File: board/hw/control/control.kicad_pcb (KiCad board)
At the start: 2 copper layers, 54.3 x 82.5 mm, 41 parts, among them J1 stepper #1, J2 stepper #2, J3 buttons, J4 power, J6 AVR-ISP-10, Q1 MMFTP84W, Q2 MMFTP84W, U1 ULN2003A, U2 ULN2003A, U3 ULN2003A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

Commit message: vias for screws moved to MountingHole, so that it's clearly visible in 3D preview
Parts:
- added ?: M3, MountingHole:MountingHole_3.2mm_M3_Pad_TopBottom, F.Cu at (125.2, 67.5)
- added ?: M3, MountingHole:MountingHole_3.2mm_M3_Pad_TopBottom, F.Cu at (171.5, 67.5)
- added ?: M3, MountingHole:MountingHole_3.2mm_M3_Pad_TopBottom, F.Cu at (171.5, 142.5)
- added ?: M3, MountingHole:MountingHole_3.2mm_M3_Pad_TopBottom, F.Cu at (125.2, 142.5)
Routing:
- net 0V: vias 10 -> 6
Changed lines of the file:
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@@
     )
+  )
+  (footprint "MountingHole:MountingHole_3.2mm_M3_Pad_TopBottom" (layer "F.Cu")
+    (at 125.1711 67.5336)
+    (descr "Mounting Hole 3.2mm, M3")
+    (tags "mounting hole 3.2mm m3")
+    (attr exclude_from_pos_files exclude_from_bom)
+    (fp_text reference "" (at 0 -4.2) (layer "F.SilkS")
+        (effects (font (size 1 1) (thickness 0.15)))
+    )
+    (fp_text value "M3" (at 0 4.2) (layer "F.Fab")
+        (effects (font (size 1 1) (thickness 0.15)))
+    )
+    (fp_text user "${REFERENCE}" (at 0 0) (layer "F.Fab")
+        (effects (font (size 1 1) (thickness 0.15)))
+    )
+    (fp_circle (center 0 0) (end 3.2 0)
+      (stroke (width 0.15) (type solid)) (fill none) (layer "Cmts.User"))
+    (fp_circle (center 0 0) (end 3.45 0)
+      (stroke (width 0.05) (type solid)) (fill none) (layer "F.CrtYd"))
+    (pad "1" thru_hole circle (at 0 0) (size 3.6 3.6) (drill 3.2) (layers "*.Cu" "*.Mask"))
+    (pad "1" connect circle (at 0 0) (size 6.4 6.4) (layers "F.Cu" "F.Mask"))
+    (pad "1" connect circle (at 0 0) (size 6.4 6.4) (layers "B.Cu" "B.Mask"))
   )
   (footprint "Resistor_SMD:R_0805_2012Metric_Pad1.20x1.40mm_HandSolder" (layer "F.Cu")
@@
       (rotate (xyz 0 0 0))
     )
+  )
+  (footprint "MountingHole:MountingHole_3.2mm_M3_Pad_TopBottom" (layer "F.Cu")
+    (at 171.5261 67.5336)
+    (descr "Mounting Hole 3.2mm, M3")
+    (tags "mounting hole 3.2mm m3")
+    (attr exclude_from_pos_files exclude_from_bom)
+    (fp_text reference "" (at 0 -4.2) (layer "F.SilkS")
+        (effects (font (size 1 1) (thickness 0.15)))
+    )
+    (fp_text value "M3" (at 0 4.2) (layer "F.Fab")
+        (effects (font (size 1 1) (thickness 0.15)))
+    )
+    (fp_text user "${REFERENCE}" (at 0 0) (layer "F.Fab")
+        (effects (font (size 1 1) (thickness 0.15)))
+    )
+    (fp_circle (center 0 0) (end 3.2 0)
+      (stroke (width 0.15) (type solid)) (fill none) (layer "Cmts.User"))
+    (fp_circle (center 0 0) (end 3.45 0)
+      (stroke (width 0.05) (type solid)) (fill none) (layer "F.CrtYd"))
+    (pad "1" thru_hole circle (at 0 0) (size 3.6 3.6) (drill 3.2) (layers "*.Cu" "*.Mask"))
+    (pad "1" connect circle (at 0 0) (size 6.4 6.4) (layers "F.Cu" "F.Mask"))
+    (pad "1" connect circle (at 0 0) (size 6.4 6.4) (layers "B.Cu" "B.Mask"))
   )
   (footprint "Capacitor_SMD:C_0805_2012Metric" (layer "F.Cu")
@@
     )
   )
+  (footprint "MountingHole:MountingHole_3.2mm_M3_Pad_TopBottom" (layer "F.Cu")
+    (at 171.5261 142.4636)
+    (descr "Mounting Hole 3.2mm, M3")
+    (tags "mounting hole 3.2mm m3")
+    (attr exclude_from_pos_files exclude_from_bom)
+    (fp_text reference "" (at 0 -4.2) (layer "F.SilkS")
+        (effects (font (size 1 1) (thickness 0.15)))
+    )
+    (fp_text value "M3" (at 0 4.2) (layer "F.Fab")
+        (effects (font (size 1 1) (thickness 0.15)))
+    )
+    (fp_text user "${REFERENCE}" (at 0 0) (layer "F.Fab")
+        (effects (font (size 1 1) (thickness 0.15)))
+    )
+    (fp_circle (center 0 0) (end 3.2 0)
+      (stroke (width 0.15) (type solid)) (fill none) (layer "Cmts.User"))
+    (fp_circle (center 0 0) (end 3.45 0)
+      (stroke (width 0.05) (type solid)) (fill none) (layer "F.CrtYd"))
+    (pad "1" thru_hole circle (at 0 0) (size 3.6 3.6) (drill 3.2) (layers "*.Cu" "*.Mask"))
+    (pad "1" connect circle (at 0 0) (size 6.4 6.4) (layers "F.Cu" "F.Mask"))
+    (pad "1" connect circle (at 0 0) (size 6.4 6.4) (layers "B.Cu" "B.Mask"))
+  )
   (footprint "Diode_SMD:D_0805_2012Metric" (layer "F.Cu")
     (at 159.4335 103.632 180)
@@
       (rotate (xyz 0 0 0))
     )
+  )
+  (footprint "MountingHole:MountingHole_3.2mm_M3_Pad_TopBottom" (layer "F.Cu")
+    (at 125.1711 142.4636)
+    (descr "Mounting Hole 3.2mm, M3")
+    (tags "mounting hole 3.2mm m3")
+    (attr exclude_from_pos_files exclude_from_bom)
+    (fp_text reference "" (at 0 -4.2) (layer "F.SilkS")
+        (effects (font (size 1 1) (thickness 0.15)))
+    )
+    (fp_text value "M3" (at 0 4.2) (layer "F.Fab")
+        (effects (font (size 1 1) (thickness 0.15)))
+    )
+    (fp_text user "${REFERENCE}" (at 0 0) (layer "F.Fab")
+        (effects (font (size 1 1) (thickness 0.15)))
+    )
+    (fp_circle (center 0 0) (end 3.2 0)
+      (stroke (width 0.15) (type solid)) (fill none) (layer "Cmts.User"))
+    (fp_circle (center 0 0) (end 3.45 0)
+      (stroke (width 0.05) (type solid)) (fill none) (layer "F.CrtYd"))
+    (pad "1" thru_hole circle (at 0 0) (size 3.6 3.6) (drill 3.2) (layers "*.Cu" "*.Mask"))
+    (pad "1" connect circle (at 0 0) (size 6.4 6.4) (layers "F.Cu" "F.Mask"))
+    (pad "1" connect circle (at 0 0) (size 6.4 6.4) (layers "B.Cu" "B.Mask"))
   )
   (footprint "Package_SO:SOIC-16_3.9x9.9mm_P1.27mm" (layer "F.Cu")
@@
   (segment (start 149.32 87.852) (end 149.352 87.884) (width 0.25) (layer "F.Cu") (net 2))
   (via (at 134.62 92.71) (size 1) (drill 0.5) (layers "F.Cu" "B.Cu") (free) (net 2))
-  (via (at 171.5261 67.5336) (size 4) (drill 3) (layers "F.Cu" "B.Cu") (net 2))
   (via (at 159.766 121.158) (size 1) (drill 0.5) (layers "F.Cu" "B.Cu") (free) (net 2))
   (via (at 161.544 113.538) (size 1) (drill 0.5) (layers "F.Cu" "B.Cu") (free) (net 2))
   (via (at 156.972 111.506) (size 0.8) (drill 0.4) (layers "F.Cu" "B.Cu") (free) (net 2))
-  (via (at 125.1711 142.4636) (size 4) (drill 3) (layers "F.Cu" "B.Cu") (net 2))
-  (via (at 125.1711 67.5336) (size 4) (drill 3) (layers "F.Cu" "B.Cu") (net 2))
   (via (at 160.02 91.44) (size 0.8) (drill 0.4) (layers "F.Cu" "B.Cu") (free) (net 2))
-  (via (at 171.5261 142.4636) (size 4) (drill 3) (layers "F.Cu" "B.Cu") (net 2))
   (via (at 149.352 87.884) (size 1) (drill 0.5) (layers "F.Cu" "B.Cu") (net 2))
   (segment (start 140.97 98.65) (end 143.51 101.19) (width 0.25) (layer "F.Cu") (net 3))

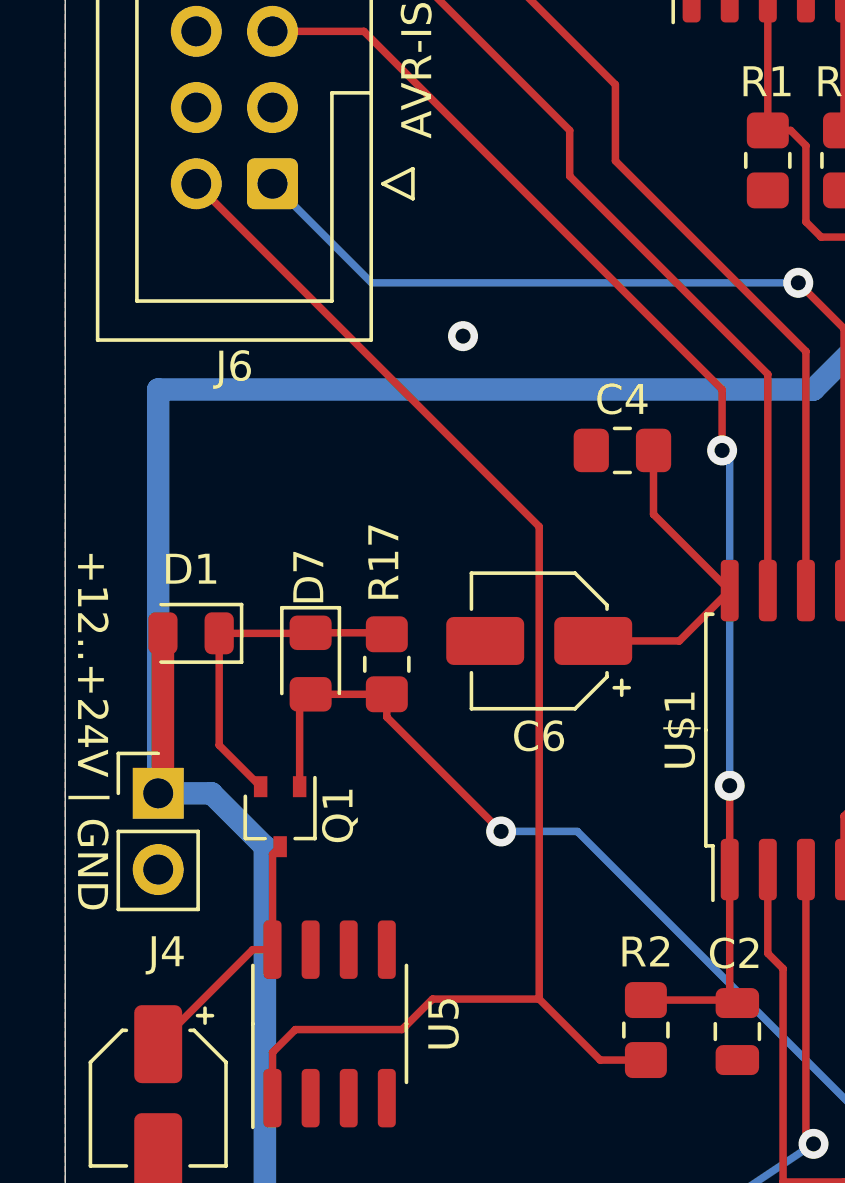
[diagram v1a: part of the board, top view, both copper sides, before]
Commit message: added mount holes instead of vias + associated mess
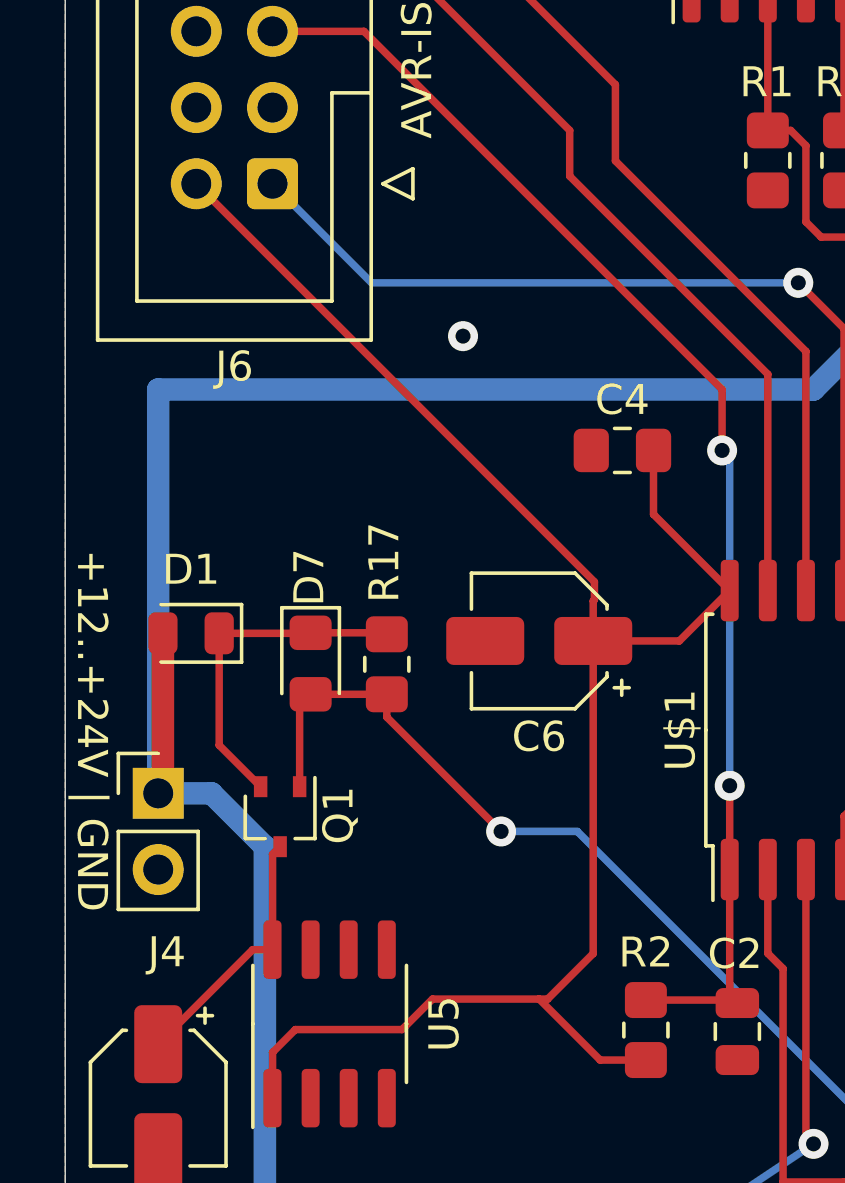
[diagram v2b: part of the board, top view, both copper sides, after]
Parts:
- gave numbers to parts that had none: 4
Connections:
- C4 pad 2: Net-(U$1-VCC) -> +5V
- C6 pad 1: Net-(U$1-VCC) -> +5V
- U$1 pad 20: Net-(U$1-VCC) -> +5V
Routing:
- net +5V: track 47.5 -> 60.1 mm
- net Net-(U$1-VCC): track 11.0 -> 0.00 mm

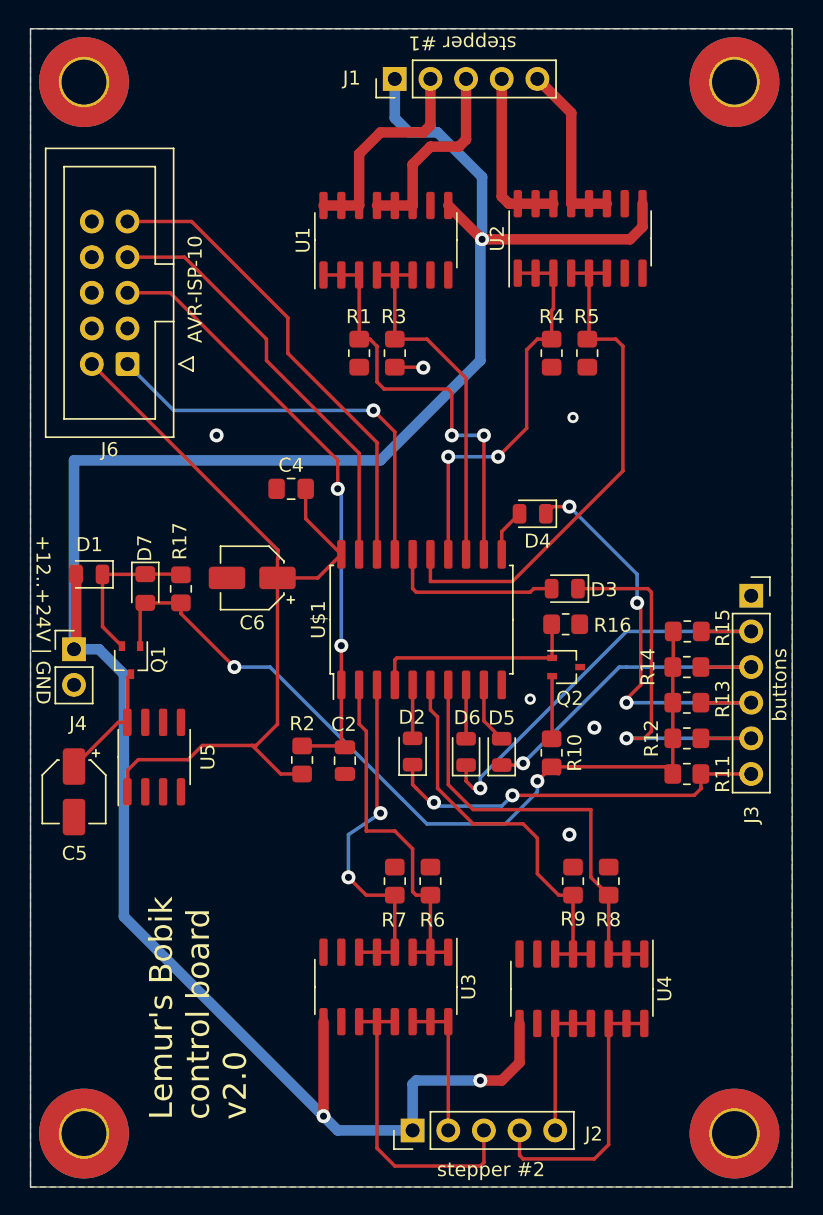
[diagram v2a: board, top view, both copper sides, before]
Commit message: mountholes adjusted to better match existing 3D mount points on the model
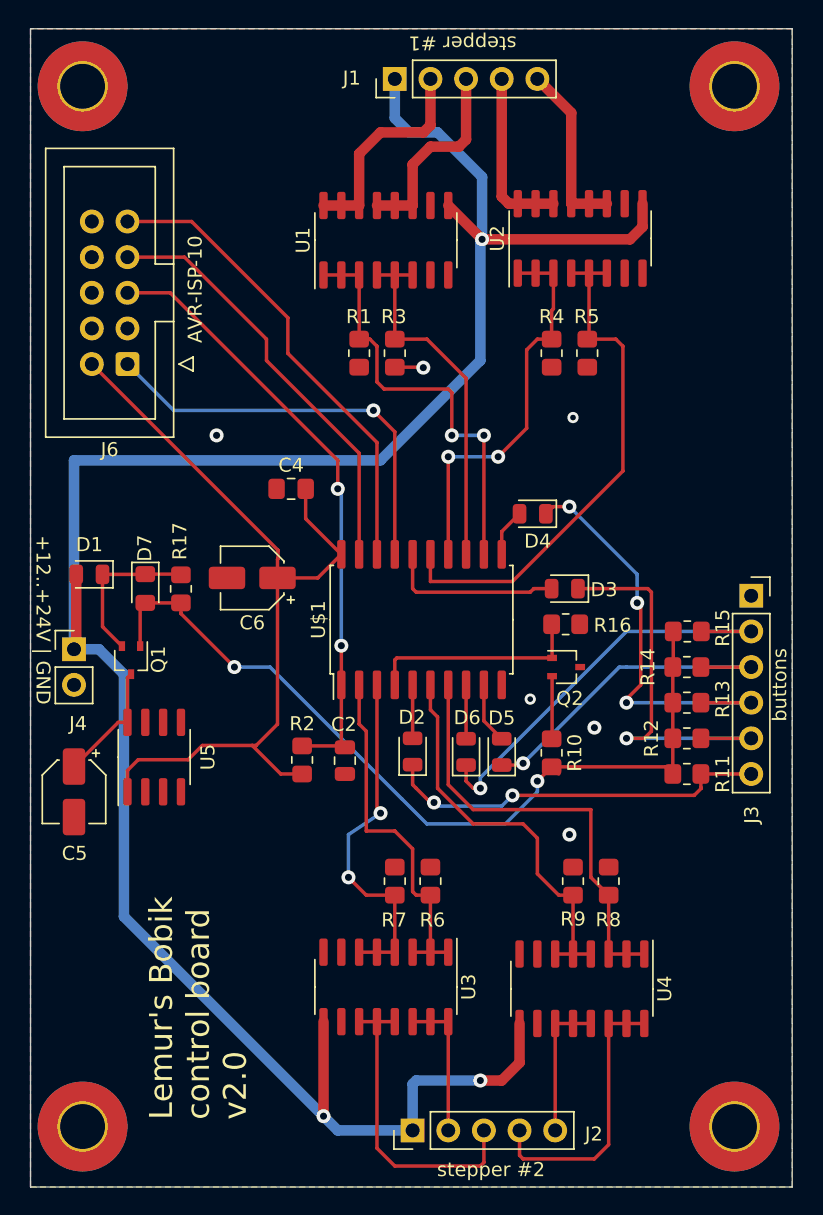
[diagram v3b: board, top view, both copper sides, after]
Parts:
- moved 3 0.51 mm to (125.1, 142.0)
- moved 4 0.50 mm to (171.5, 142.0)
- moved 1 0.32 mm to (125.1, 67.8)
- moved 2 0.30 mm to (171.5, 67.8)
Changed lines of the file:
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@@
   )
   (footprint "MountingHole:MountingHole_3.2mm_M3_Pad_TopBottom" (layer "F.Cu")
-    (at 125.1711 67.5336)
+    (at 125.0711 67.8336)
     (descr "Mounting Hole 3.2mm, M3")
     (tags "mounting hole 3.2mm m3")
@@
   )
   (footprint "MountingHole:MountingHole_3.2mm_M3_Pad_TopBottom" (layer "F.Cu")
-    (at 171.5261 67.5336)
+    (at 171.5261 67.8336)
     (descr "Mounting Hole 3.2mm, M3")
     (tags "mounting hole 3.2mm m3")
@@
   )
   (footprint "MountingHole:MountingHole_3.2mm_M3_Pad_TopBottom" (layer "F.Cu")
-    (at 171.5261 142.4636)
+    (at 171.5261 141.9636)
     (descr "Mounting Hole 3.2mm, M3")
     (tags "mounting hole 3.2mm m3")
@@
   )
   (footprint "MountingHole:MountingHole_3.2mm_M3_Pad_TopBottom" (layer "F.Cu")
-    (at 125.1711 142.4636)
+    (at 125.0711 141.9636)
     (descr "Mounting Hole 3.2mm, M3")
     (tags "mounting hole 3.2mm m3")
